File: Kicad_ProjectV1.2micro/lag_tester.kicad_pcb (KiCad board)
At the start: 2 copper layers, 72 x 43 mm, 56 parts, among them J1 HDMI_A, J2 USB_B_Mini, J3 AVR-JTAG-10, SW1 SW_Coded, U1 10M02SCE144I7G, U2 TC1264-3.3VDBTR, U3 TFP410PAP, X1 CXO_DIP8

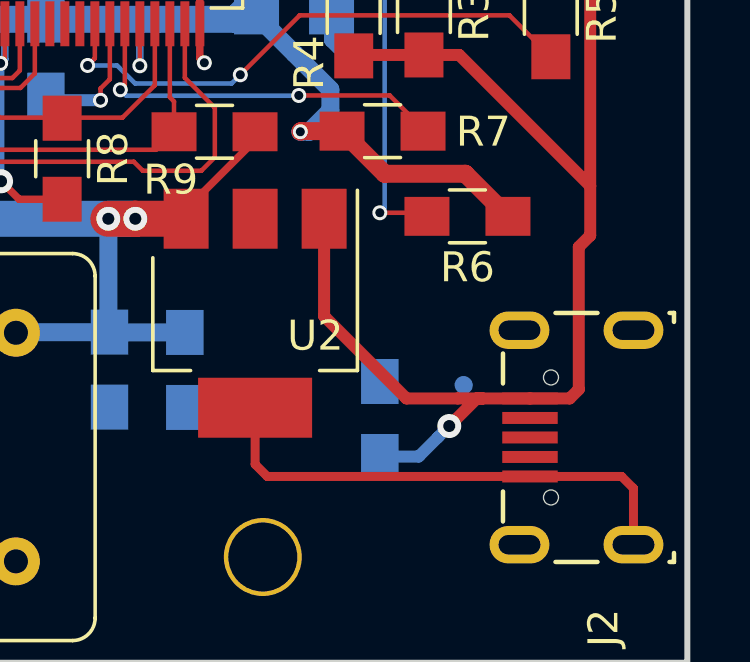
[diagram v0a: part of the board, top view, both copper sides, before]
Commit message: Fix USB Micro B footprint pin assignment and add gerbers
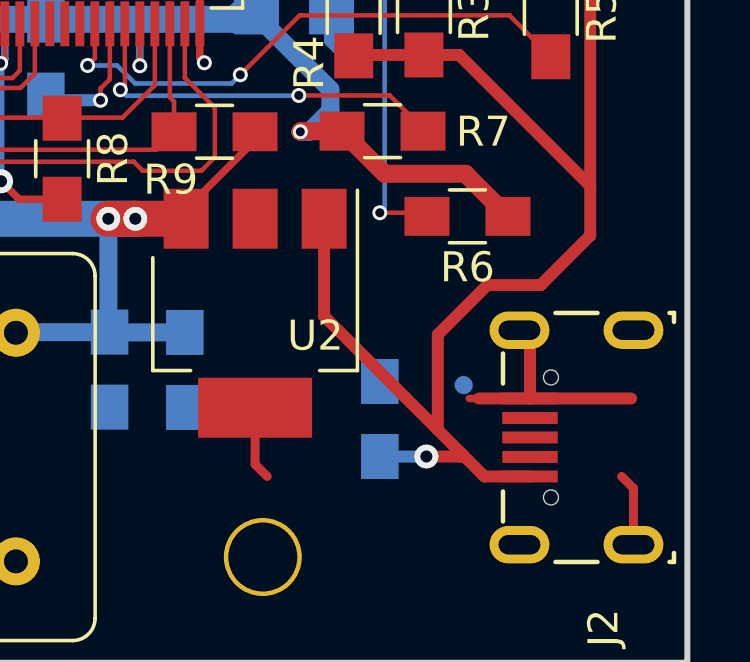
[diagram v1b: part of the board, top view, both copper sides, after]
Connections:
- J2 pad 1: /GND -> /+5
- J2 pad 5: /+5 -> /GND
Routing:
- net /GND: track 103.3 -> 99.3 mm
- net /+5: track 49.2 -> 51.4 mm
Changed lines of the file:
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@@
     (thickness 1.6)
     (drawings 5)
-    (tracks 748)
+    (tracks 751)
     (zones 0)
     (modules 56)
@@
     (mod_text_size 1 1)
     (mod_text_width 0.15)
-    (pad_size 8 8)
+    (pad_size 0.4 1.85)
     (pad_drill 0)
     (pad_to_mask_clearance 0.2)
@@
       (drillshape 0)
       (scaleselection 1)
-      (outputdirectory "Gerber"))
+      (outputdirectory "GRB/"))
   )
   (net 0 "")
@@
       (effects (font (size 0.25 0.25) (thickness 0.0625)))
     )
-    (fp_text user "PCB Edge" (at 0 3.75 90) (layer Dwgs.User)
-      (effects (font (size 0.5 0.5) (thickness 0.08)))
-    )
-    (fp_text user %R (at -5.7 -0.075 270) (layer F.Fab)
-      (effects (font (size 1 1) (thickness 0.15)))
-    )
     (fp_line (start -4 -2.25) (end -4 3.15) (layer F.Fab) (width 0.15))
     (fp_line (start -4 3.15) (end -3.7 3.15) (layer F.Fab) (width 0.15))
@@
     (fp_line (start 4.95 4.85) (end 4.95 -3.34) (layer F.CrtYd) (width 0.05))
     (fp_line (start 4.95 -3.34) (end -4.94 -3.34) (layer F.CrtYd) (width 0.05))
+    (fp_text user "PCB Edge" (at 0 3.75 90) (layer Dwgs.User)
+      (effects (font (size 0.5 0.5) (thickness 0.08)))
+    )
+    (fp_text user %R (at -5.7 -0.075 270) (layer F.Fab)
+      (effects (font (size 1 1) (thickness 0.15)))
+    )
     (pad "" np_thru_hole oval (at 2 -0.8 90) (size 0.5 0.5) (drill 0.5) (layers *.Cu *.Mask))
     (pad "" np_thru_hole oval (at -2 -0.8 90) (size 0.5 0.5) (drill 0.5) (layers *.Cu *.Mask))
@@
       (net 14 /GND))
     (pad 5 smd rect (at 1.3 -1.5 90) (size 0.4 1.85) (layers F.Cu F.Paste F.Mask)
-      (net 15 /+5))
+      (net 14 /GND))
     (pad 4 smd rect (at 0.65 -1.5 90) (size 0.4 1.85) (layers F.Cu F.Paste F.Mask)
       (net 16 "Net-(J2-Pad4)"))
@@
       (net 17 "Net-(J2-Pad2)"))
     (pad 1 smd rect (at -1.3 -1.5 90) (size 0.4 1.85) (layers F.Cu F.Paste F.Mask)
-      (net 14 /GND))
+      (net 15 /+5))
     (model ${KISYS3DMOD}/Connectors_USB.3dshapes/USB_Micro-B_Wuerth-629105150521.wrl
       (at (xyz 0 0 0))
@@
   (segment (start 73.41 101.45) (end 73.41 101.5) (width 0.25) (layer B.Cu) (net 14))
   (segment (start 73.41 101.5) (end 70.9 104.01) (width 0.25) (layer B.Cu) (net 14))
-  (segment (start 133.755 111.79) (end 124.998 111.79) (width 0.3) (layer F.Cu) (net 14))
   (segment (start 124.592782 111.384782) (end 124.592782 109.499344) (width 0.3) (layer F.Cu) (net 14))
   (segment (start 124.998 111.79) (end 124.592782 111.384782) (width 0.3) (layer F.Cu) (net 14))
-  (segment (start 133.755 111.79) (end 136.809 111.79) (width 0.3) (layer F.Cu) (net 14))
   (segment (start 137.205 112.186) (end 137.205 114.065) (width 0.3) (layer F.Cu) (net 14))
   (segment (start 136.809 111.79) (end 137.205 112.186) (width 0.3) (layer F.Cu) (net 14))
   (segment (start 117.79 99.25) (end 117.62 99.08) (width 0.4) (layer B.Cu) (net 14))
   (segment (start 119.44 99.25) (end 117.79 99.25) (width 0.4) (layer B.Cu) (net 14))
+  (segment (start 133.755 109.19) (end 132.05 109.19) (width 0.4) (layer F.Cu) (net 14))
+  (segment (start 132.05 109.19) (end 131.729 109.19) (width 0.25) (layer F.Cu) (net 14))
+  (segment (start 133.755 107.265) (end 133.405 106.915) (width 0.4) (layer F.Cu) (net 14))
+  (segment (start 133.755 109.19) (end 133.755 107.265) (width 0.4) (layer F.Cu) (net 14))
+  (segment (start 133.755 109.19) (end 137.13 109.19) (width 0.4) (layer F.Cu) (net 14))
   (segment (start 135.763 102.108) (end 135.763 102.235) (width 0.3) (layer F.Cu) (net 15))
   (segment (start 126.892782 103.199344) (end 126.892782 106.445782) (width 0.4) (layer F.Cu) (net 15))
@@
   (segment (start 135.763 102.108) (end 135.763 92.338) (width 0.4) (layer F.Cu) (net 15))
   (segment (start 135.763 92.338) (end 131.925 88.5) (width 0.4) (layer F.Cu) (net 15))
-  (segment (start 131.348 109.19) (end 129.637 109.19) (width 0.4) (layer F.Cu) (net 15))
   (segment (start 128.75 111.125) (end 130.048 111.125) (width 0.4) (layer B.Cu) (net 15))
-  (segment (start 130.048 111.125) (end 130.683 110.49) (width 0.4) (layer B.Cu) (net 15))
-  (segment (start 135.382 104.14) (end 135.763 103.759) (width 0.4) (layer F.Cu) (net 15))
-  (segment (start 135.763 103.759) (end 135.763 102.108) (width 0.4) (layer F.Cu) (net 15))
-  (segment (start 133.755 109.19) (end 135.08 109.19) (width 0.4) (layer F.Cu) (net 15))
-  (segment (start 135.08 109.19) (end 135.382 108.888) (width 0.4) (layer F.Cu) (net 15))
-  (segment (start 135.382 108.888) (end 135.382 104.14) (width 0.4) (layer F.Cu) (net 15))
-  (via (at 131.064 110.109) (size 0.8) (drill 0.4) (layers F.Cu B.Cu) (net 15))
-  (segment (start 130.683 110.49) (end 131.064 110.109) (width 0.4) (layer B.Cu) (net 15))
-  (segment (start 131.983 109.19) (end 132.177 109.19) (width 0.4) (layer F.Cu) (net 15))
-  (segment (start 131.064 110.109) (end 131.983 109.19) (width 0.4) (layer F.Cu) (net 15))
-  (segment (start 133.755 109.19) (end 132.177 109.19) (width 0.4) (layer F.Cu) (net 15))
-  (segment (start 132.177 109.19) (end 131.348 109.19) (width 0.4) (layer F.Cu) (net 15))
+  (via (at 130.302 111.125) (size 0.8) (drill 0.4) (layers F.Cu B.Cu) (net 15))
+  (segment (start 130.048 111.125) (end 130.302 111.125) (width 0.25) (layer B.Cu) (net 15))
+  (segment (start 132.237 111.79) (end 133.755 111.79) (width 0.4) (layer F.Cu) (net 15))
+  (segment (start 131.5085 111.0615) (end 132.237 111.79) (width 0.4) (layer F.Cu) (net 15))
+  (segment (start 131.445 111.125) (end 131.5085 111.0615) (width 0.4) (layer F.Cu) (net 15))
+  (segment (start 130.302 111.125) (end 131.445 111.125) (width 0.4) (layer F.Cu) (net 15))
+  (segment (start 130.683 107.061) (end 130.683 110.236) (width 0.4) (layer F.Cu) (net 15))
+  (segment (start 132.334 105.41) (end 130.683 107.061) (width 0.4) (layer F.Cu) (net 15))
+  (segment (start 131.5085 111.0615) (end 130.683 110.236) (width 0.4) (layer F.Cu) (net 15))
+  (segment (start 135.763 103.759) (end 134.112 105.41) (width 0.4) (layer F.Cu) (net 15))
+  (segment (start 130.683 110.236) (end 129.637 109.19) (width 0.4) (layer F.Cu) (net 15))
+  (segment (start 135.763 102.108) (end 135.763 103.759) (width 0.4) (layer F.Cu) (net 15))
+  (segment (start 134.112 105.41) (end 132.334 105.41) (width 0.4) (layer F.Cu) (net 15))
   (segment (start 102.86 81.8) (end 102.63 82.03) (width 0.25) (layer F.Cu) (net 18))
   (segment (start 89.2 79.85) (end 89.2 77.51) (width 0.25) (layer F.Cu) (net 18))
